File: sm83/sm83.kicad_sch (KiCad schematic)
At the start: 0 parts

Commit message: SM83: Add decoder1 schematic
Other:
- added sheet DECODER1 (decoder1.kicad_sch)
- sheet SEQUENCER ports: added IN_INTR, TABLE_CB, ~{DATA_PHASE}, ~{MCYC[0..2]}; removed MCYC_BUF2, ~{DATA_PHASE_BUF}

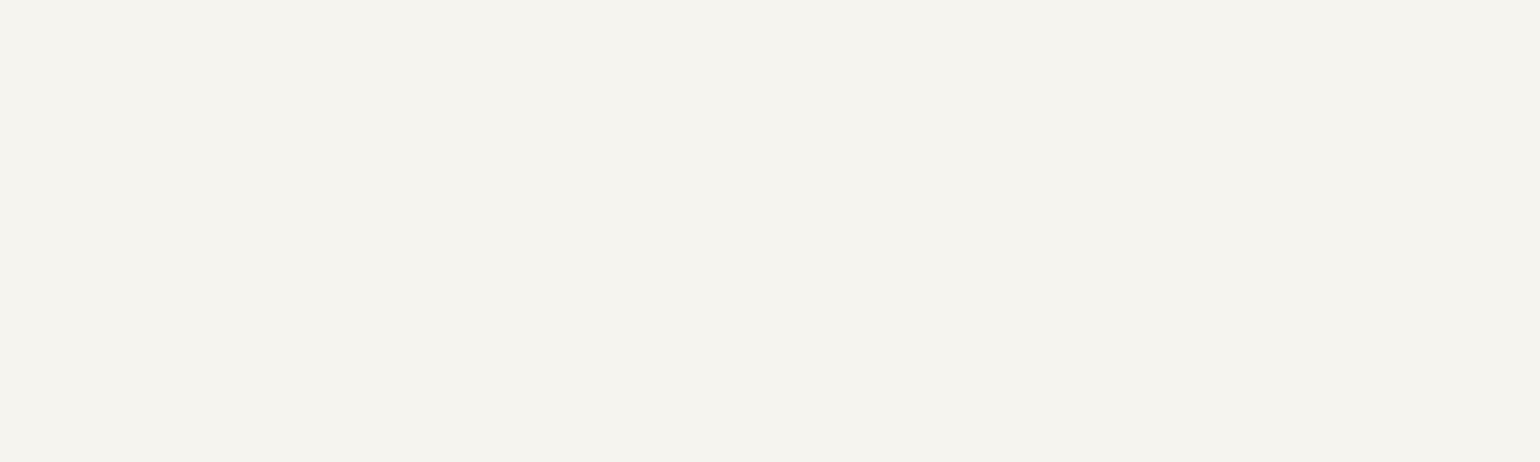
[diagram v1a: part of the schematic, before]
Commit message: SM83: Add schematic of decoder2
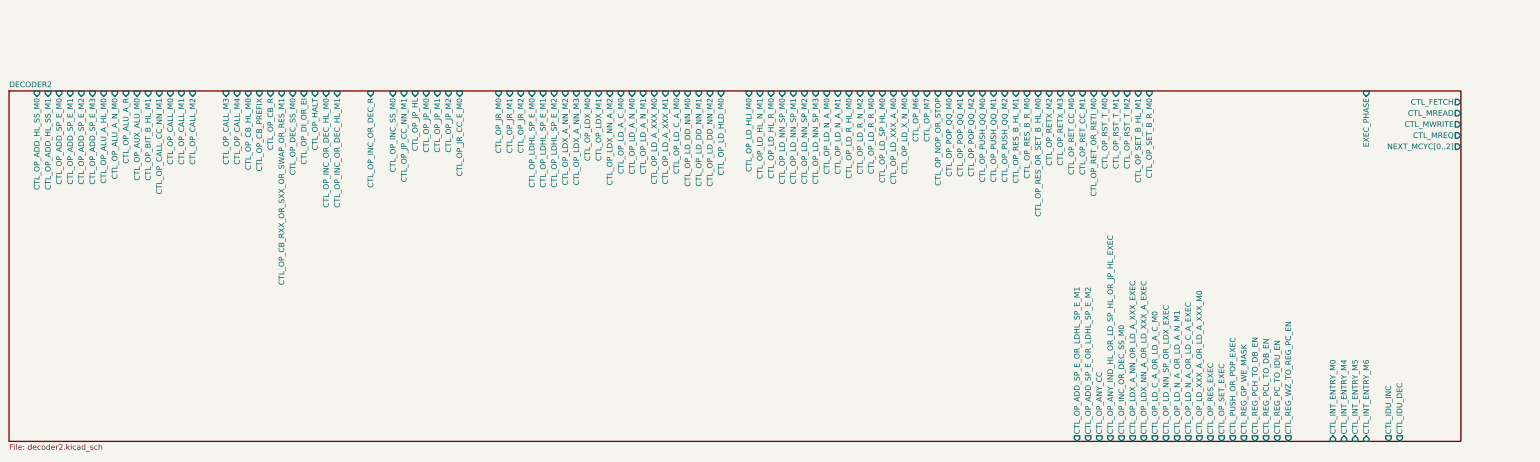
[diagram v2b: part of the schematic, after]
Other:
- added sheet DECODER2 (decoder2.kicad_sch)

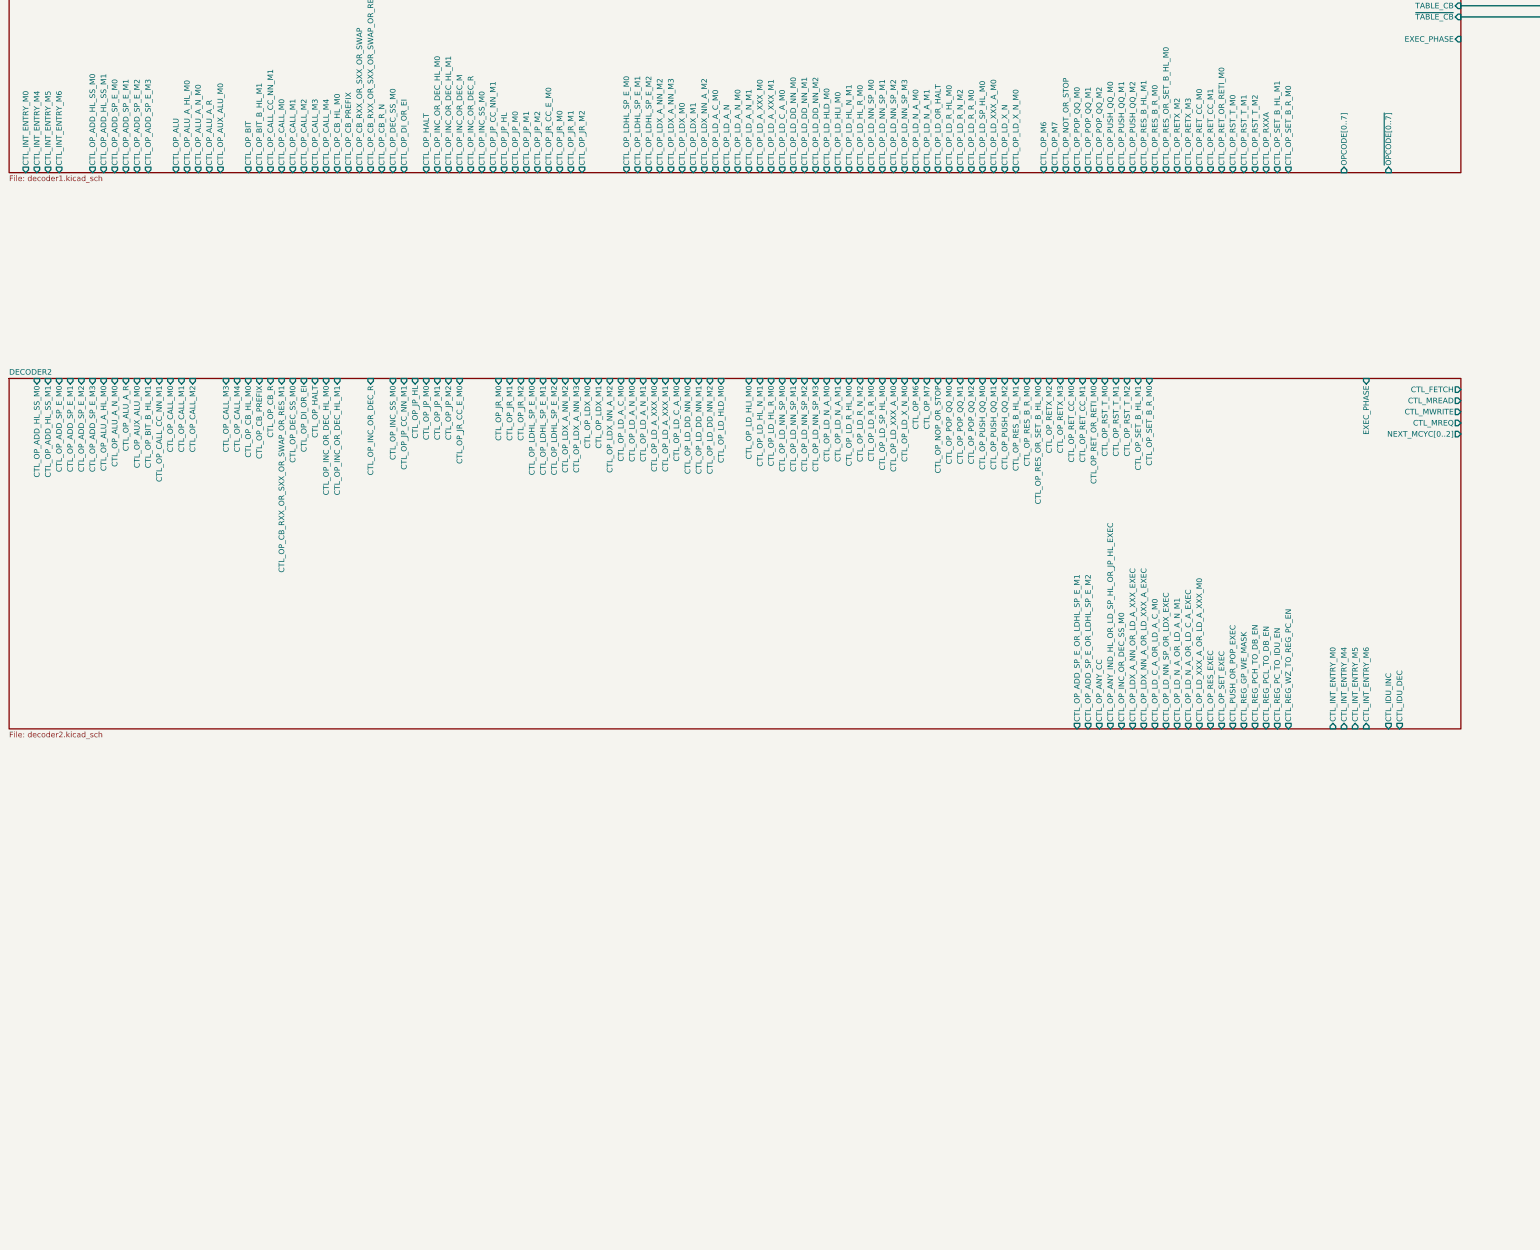
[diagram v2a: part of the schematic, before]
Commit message: SM83: Add schematic for decoder3
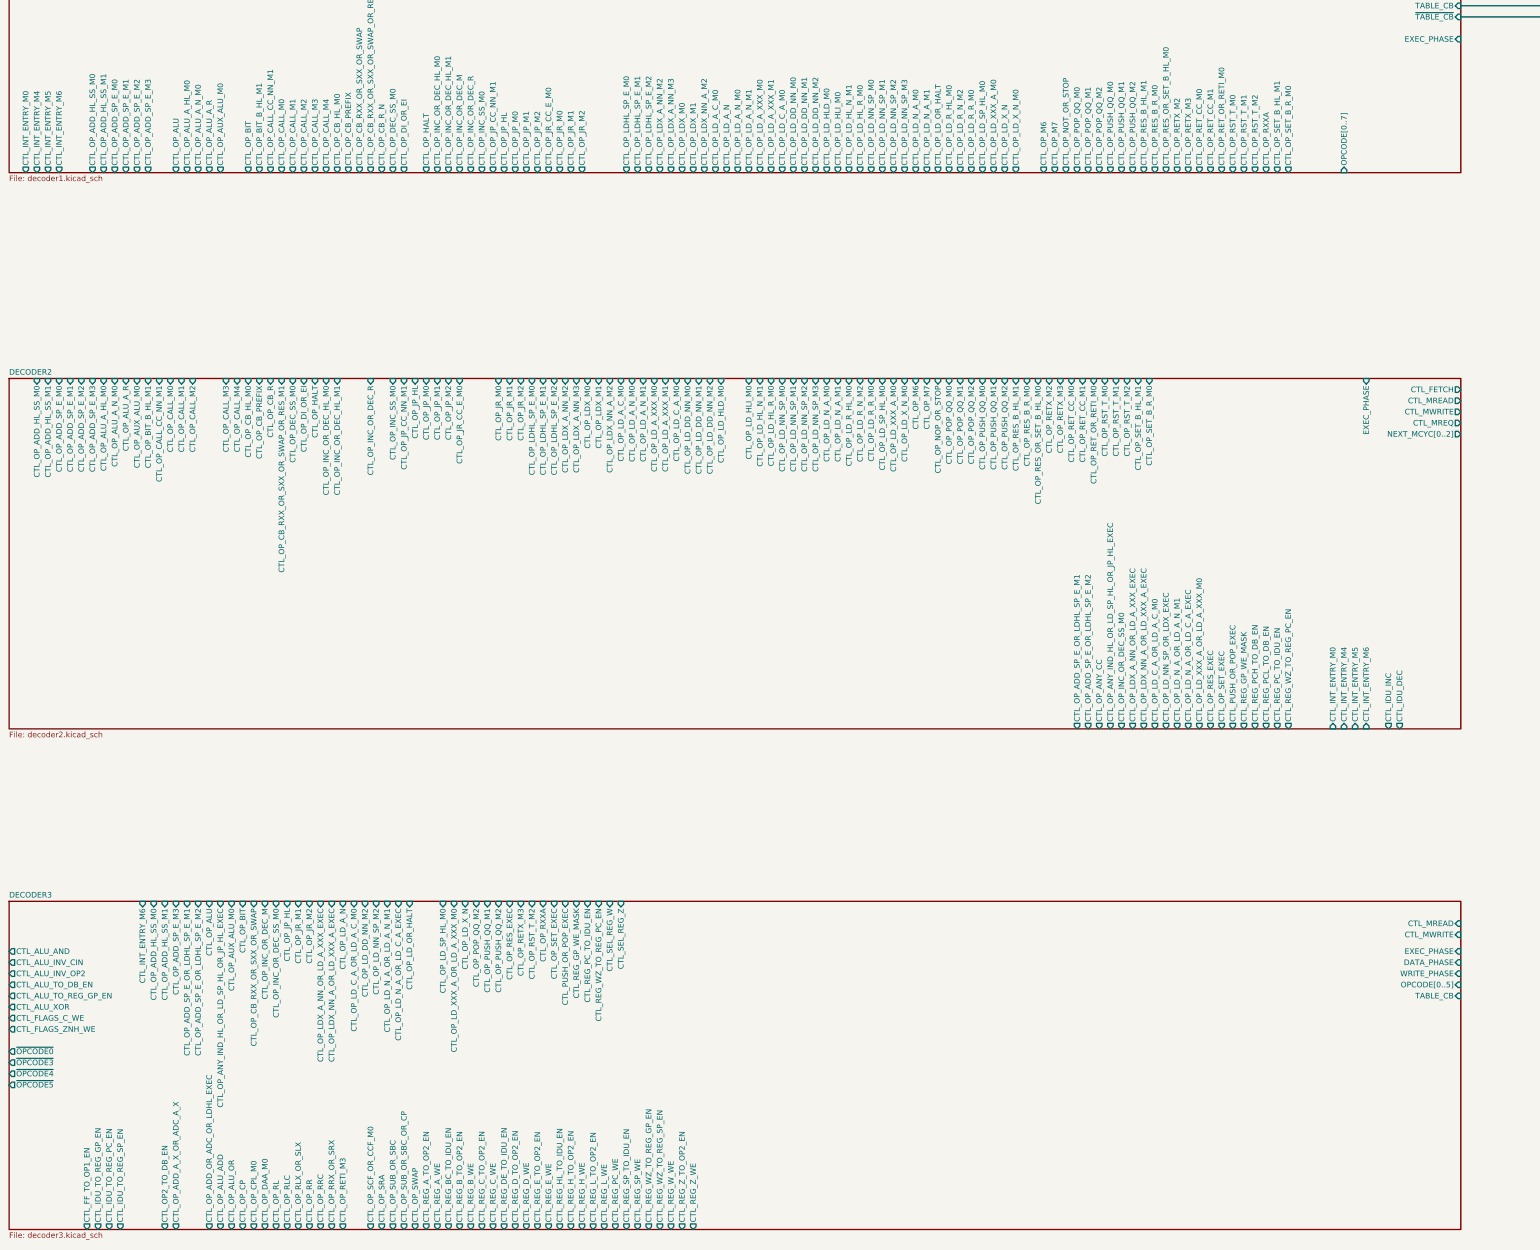
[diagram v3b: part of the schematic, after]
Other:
- added sheet DECODER3 (decoder3.kicad_sch)
- sheet DECODER1 ports: added none; removed ~{OPCODE[0..7]}

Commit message: SM83: Add schematic of ALU
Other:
- added sheet ALU (alu.kicad_sch)

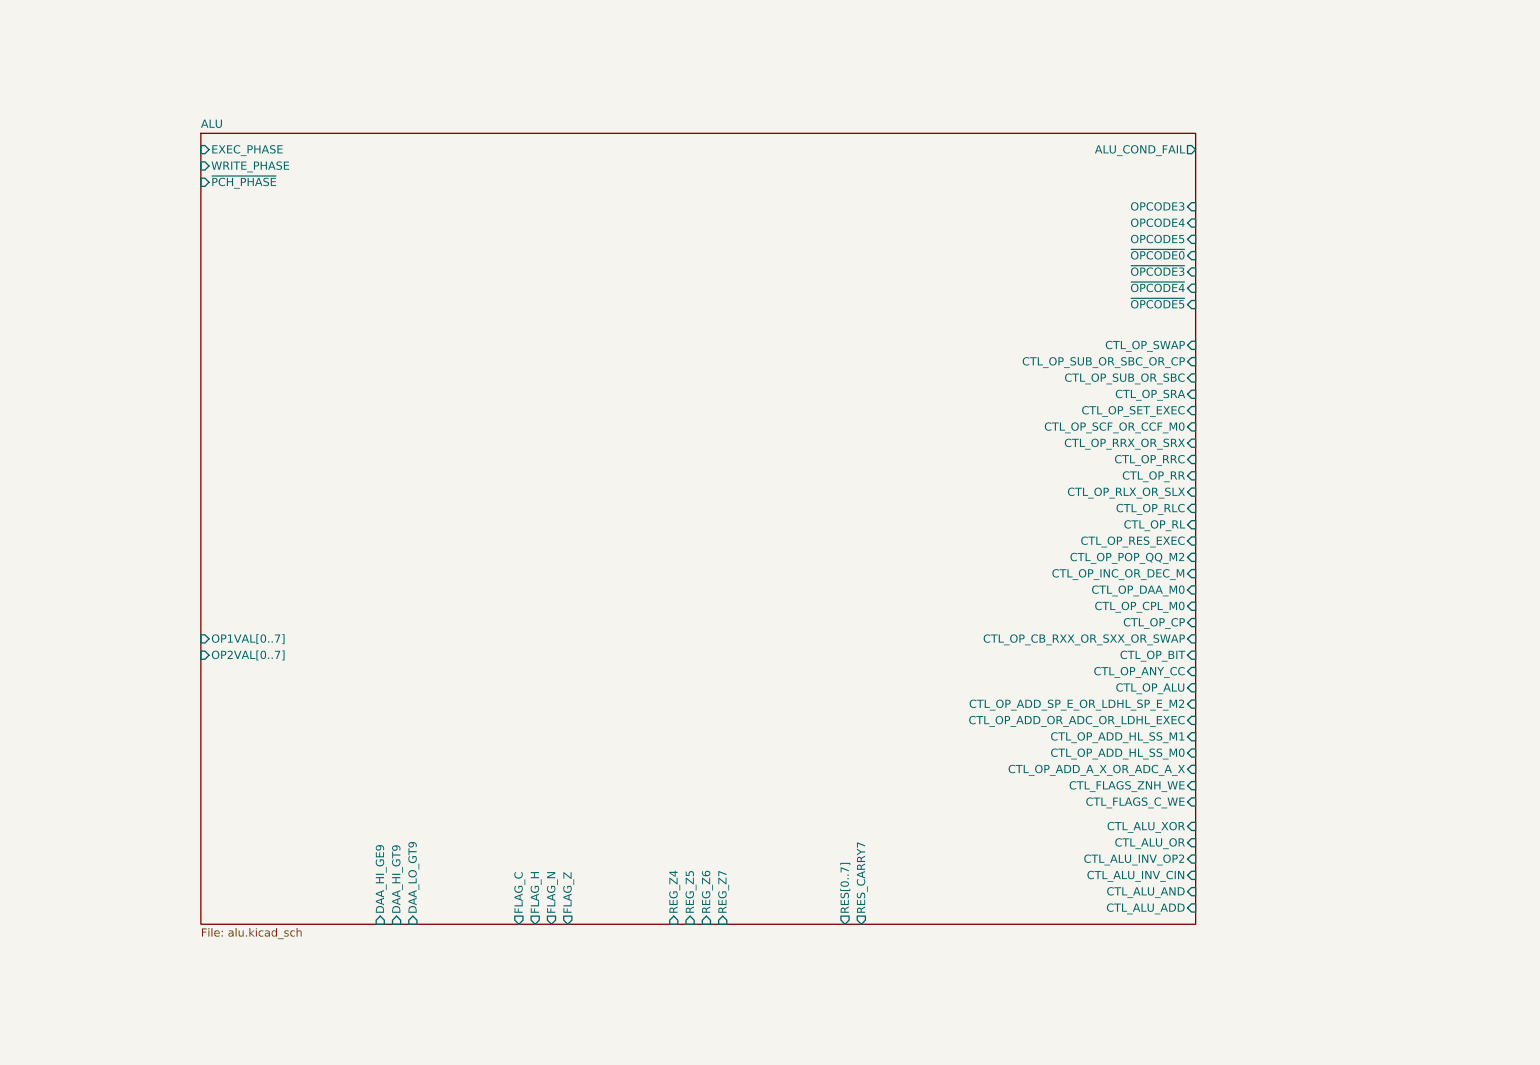
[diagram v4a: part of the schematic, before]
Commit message: SM83: Add data bus bridge schematic
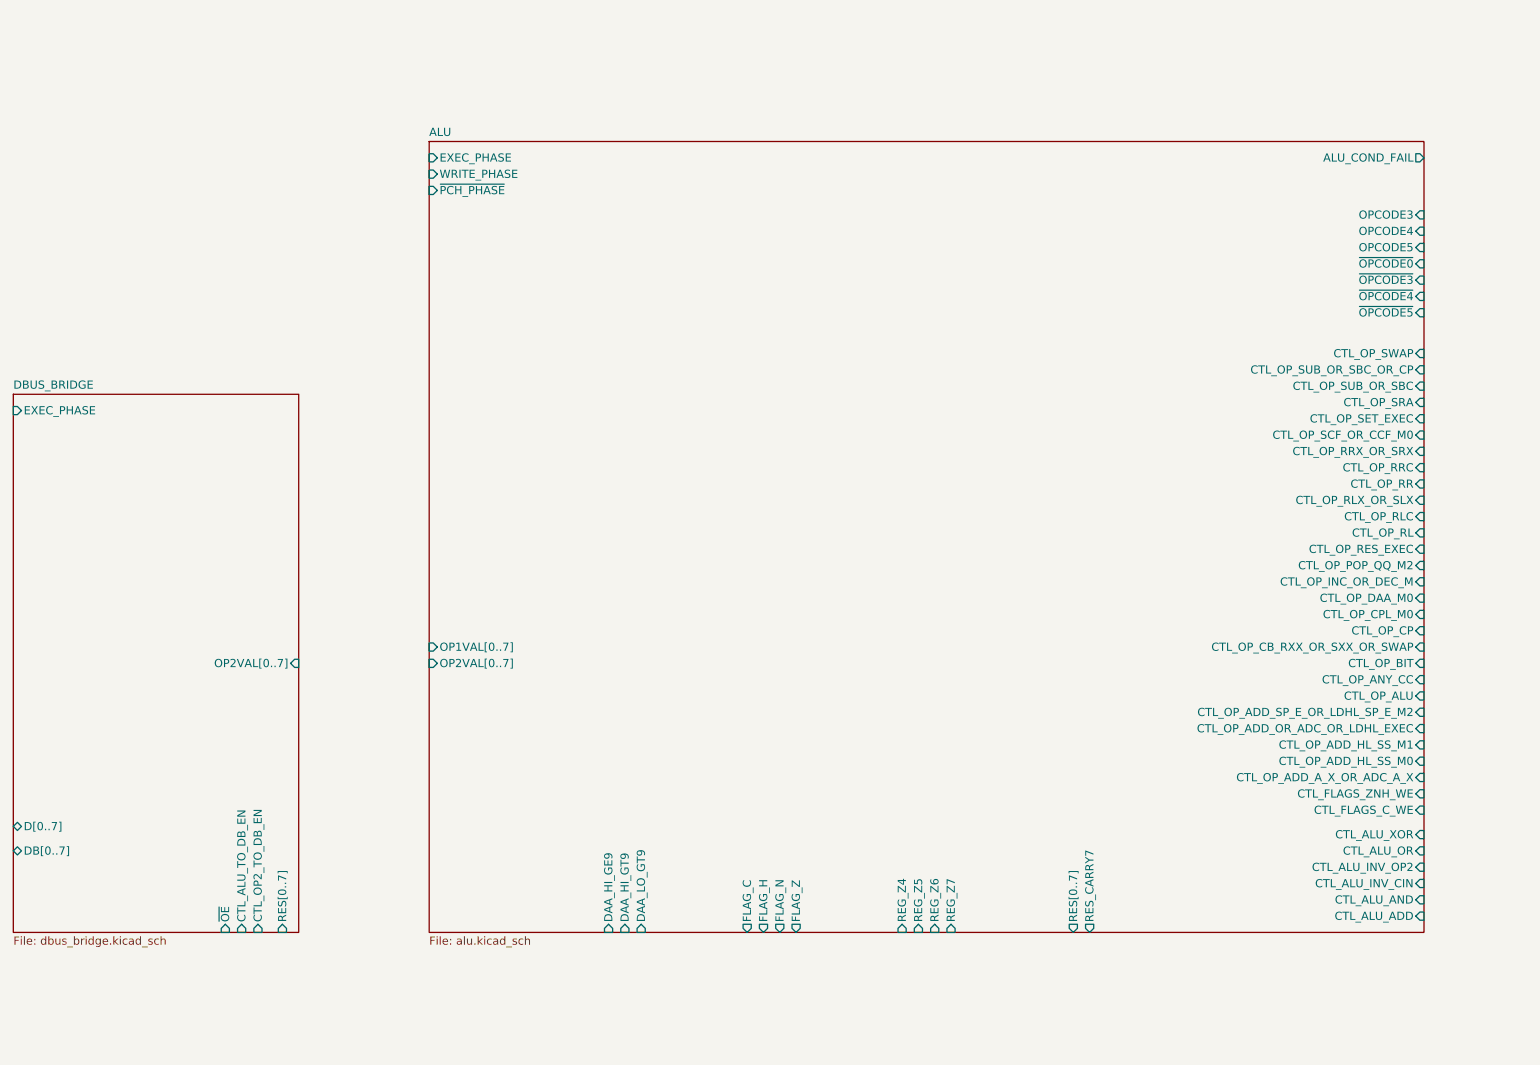
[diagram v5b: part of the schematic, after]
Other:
- added sheet DBUS_BRIDGE (dbus_bridge.kicad_sch)
